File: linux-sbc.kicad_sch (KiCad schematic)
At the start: 9 parts, among them J101 Molex Mini-fit Jr

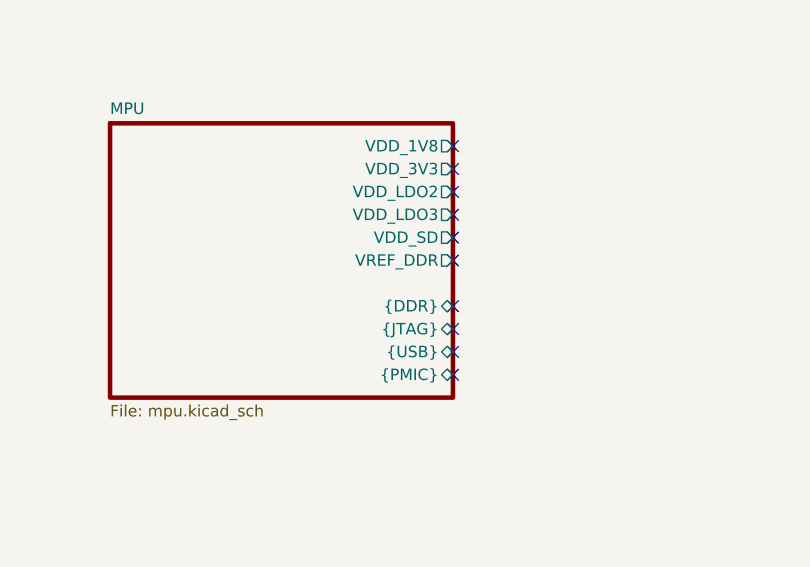
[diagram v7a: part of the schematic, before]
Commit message: Add MPU boot selection
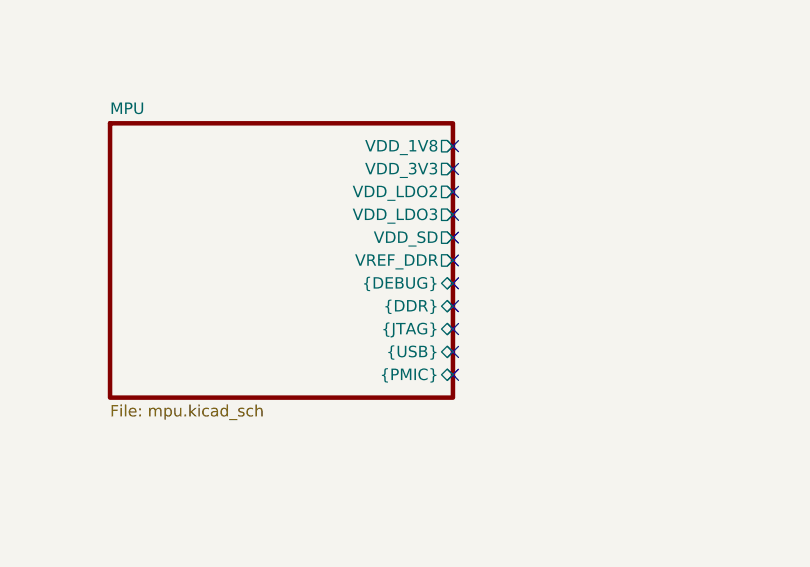
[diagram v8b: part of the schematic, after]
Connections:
- no-connect marks 10 -> 11
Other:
- sheet MPU ports: added {DEBUG}; removed none
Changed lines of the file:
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@@
+	)
+	(no_connect
+		(at 254 144.78)
 	)
 	(no_connect
@@
 			(effects
 				(font
+					(size 1.27 1.27)
+				)
+				(justify right)
+			)
+		)
+		(pin "{DEBUG}" bidirectional
+			(at 254 144.78 0)
+			(effects
+				(font
